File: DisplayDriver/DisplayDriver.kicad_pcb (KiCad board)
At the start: 2 copper layers, 1 part, among them U6 CH340N

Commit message: Design Doc 2 Final
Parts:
- removed U6: CH340N, Package_SO:SOP-8_3.9x4.9mm_P1.27mm
- added BOOT_SW: SW_Push_1P1T_NO_CK_PTS125Sx43PSMTR, Button_Switch_SMD:SW_Push_1P1T_NO_CK_PTS125Sx43PSMTR, F.Cu at (117.5, 38.5)
- added DOWN SW: SW_TL3330AF260QG, DisplayDriver:SW_TL3330AF260QG, F.Cu at (145.0, 69.5)
- added REF**: SOIC-20W_7.5x12.8mm_P1.27mm, Package_SO:SOIC-20W_7.5x12.8mm_P1.27mm, F.Cu at (70.8, 91.4)
- added REF**: LED_WS2812B_PLCC4_5.0x5.0mm_P3.2mm, LED_SMD:LED_WS2812B_PLCC4_5.0x5.0mm_P3.2mm, F.Cu at (173.5, 92.5)
- added REF**: LED_0603_1608Metric, LED_SMD:LED_0603_1608Metric, F.Cu at (240.5, 91.5)
- added REF**: SOIC-20W_7.5x12.8mm_P1.27mm, Package_SO:SOIC-20W_7.5x12.8mm_P1.27mm, F.Cu at (39.9, 91.9)
- added REF**: JST_PH_S3B-PH-K_1x03_P2.00mm_Horizontal, Connector_JST:JST_PH_S3B-PH-K_1x03_P2.00mm_Horizontal, F.Cu at (128.0, 91.5)
- added REF**: XCVR_ESP32-WROVER-B__16MB_, DisplayDriver:XCVR_ESP32-WROVER-B__16MB_, F.Cu at (47.0, 173.3)
- added REF**: IDC-Header_2x08_P2.54mm_Latch_Vertical, Connector_IDC:IDC-Header_2x08_P2.54mm_Latch_Vertical, F.Cu at (266.7, 31.1)
- added REF**: LED_0603_1608Metric, LED_SMD:LED_0603_1608Metric, F.Cu at (221.5, 91.5)
- added REF**: LED_0603_1608Metric, LED_SMD:LED_0603_1608Metric, F.Cu at (201.5, 91.5)
- added REF**: IDC-Header_2x08_P2.54mm_Latch_Vertical, Connector_IDC:IDC-Header_2x08_P2.54mm_Latch_Vertical, F.Cu at (108.0, 151.7)
- added REF**: PinHeader_1x11_P2.54mm_Vertical, Connector_PinHeader_2.54mm:PinHeader_1x11_P2.54mm_Vertical, F.Cu at (269.5, 74.7)
- added RESET SW: SW_TL3330AF260QG, DisplayDriver:SW_TL3330AF260QG, F.Cu at (173.6, 70.5)
- added UP SW: SW_TL3330AF260QG, DisplayDriver:SW_TL3330AF260QG, F.Cu at (119.5, 69.5)

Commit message: PCB commit pls
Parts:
- removed the REF** at (266.7, 31.1)
- removed the REF** at (108.0, 151.7)
- removed the REF** at (269.5, 74.7)
- added C2: C_0201_0603Metric, Capacitor_SMD:C_0201_0603Metric, F.Cu at (135.9, 42.9)
- added J1: SAMTEC_HTSS-108-01-G-D, DisplayDriver:SAMTEC_HTSS-108-01-G-D, F.Cu at (144.0, 143.0)
- added J2: PinHeader_1x11_P2.54mm_Vertical, Connector_PinHeader_2.54mm:PinHeader_1x11_P2.54mm_Vertical, F.Cu at (24.5, 140.7)
- added J3: SAMTEC_HTSS-108-01-G-D, DisplayDriver:SAMTEC_HTSS-108-01-G-D, F.Cu at (160.5, 174.4)
- added R1: R_0201_0603Metric, Resistor_SMD:R_0201_0603Metric, F.Cu at (135.9, 37.9)
- added R3: 10k, Resistor_SMD:R_0201_0603Metric, F.Cu at (97.2, 145.5)
- added SJ1: SolderJumper-3_P1.3mm_Open_Rounded, Jumper:SolderJumper-3_P1.3mm_Open_RoundedPad1.0x1.5mm_NumberLabels, F.Cu at (162.7, 150.5)
- added SJ2: SolderJumper-3_P1.3mm_Open_Rounded, Jumper:SolderJumper-3_P1.3mm_Open_RoundedPad1.0x1.5mm_NumberLabels, F.Cu at (90.2, 114.0)
- 3.3V LED-G: renamed from REF**
- 5V LED-G: renamed from REF**
- D15 LED-R: renamed from REF**
- DOWN1: renamed from DOWN SW
- RST1: renamed from RESET SW
- UP1: renamed from UP SW
- moved D15 LED-R 170.0 mm to (75.5, 50.5), turned to 90 degrees
- moved RST1 151.2 mm to (23.1, 84.6), turned to -90 degrees
- moved DOWN1 126.8 mm to (23.1, 104.6), turned to -90 degrees
- moved REF** 105.1 mm to (45.0, 27.0), turned to -90 degrees
- moved UP1 99.5 mm to (23.2, 94.6), turned to -90 degrees
- moved U1 83.7 mm to (70.5, 92.9)
- moved U3 76.9 mm to (111.0, 121.0)
- moved 5V LED-G 73.8 mm to (150.5, 71.5), turned to 90 degrees
- moved 3.3V LED-G 59.4 mm to (150.5, 61.0), turned to 90 degrees
- moved U2 40.6 mm to (111.2, 96.6)
- moved SW1 30.6 mm to (119.8, 69.0)
- moved neo_LED 20.9 mm to (178.7, 72.3), turned to -90 degrees
- renumbered BOOT_SW to SW1, REF** to U1, REF** to U2, REF** to U3, REF** to neo_LED
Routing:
- net (no net): track 0.00 -> 1102.3 mm

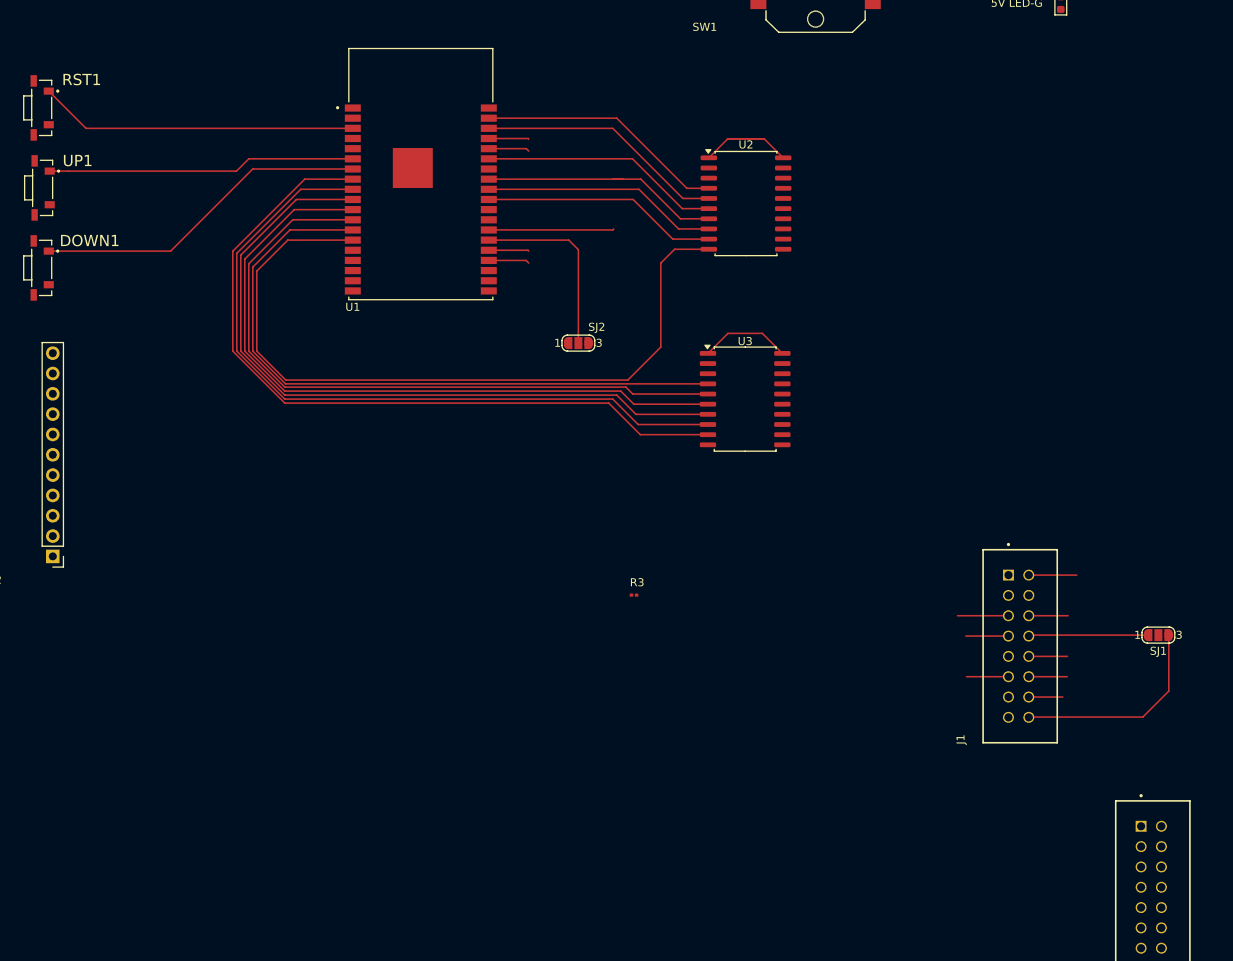
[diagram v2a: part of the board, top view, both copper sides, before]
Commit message: desktop to laptop
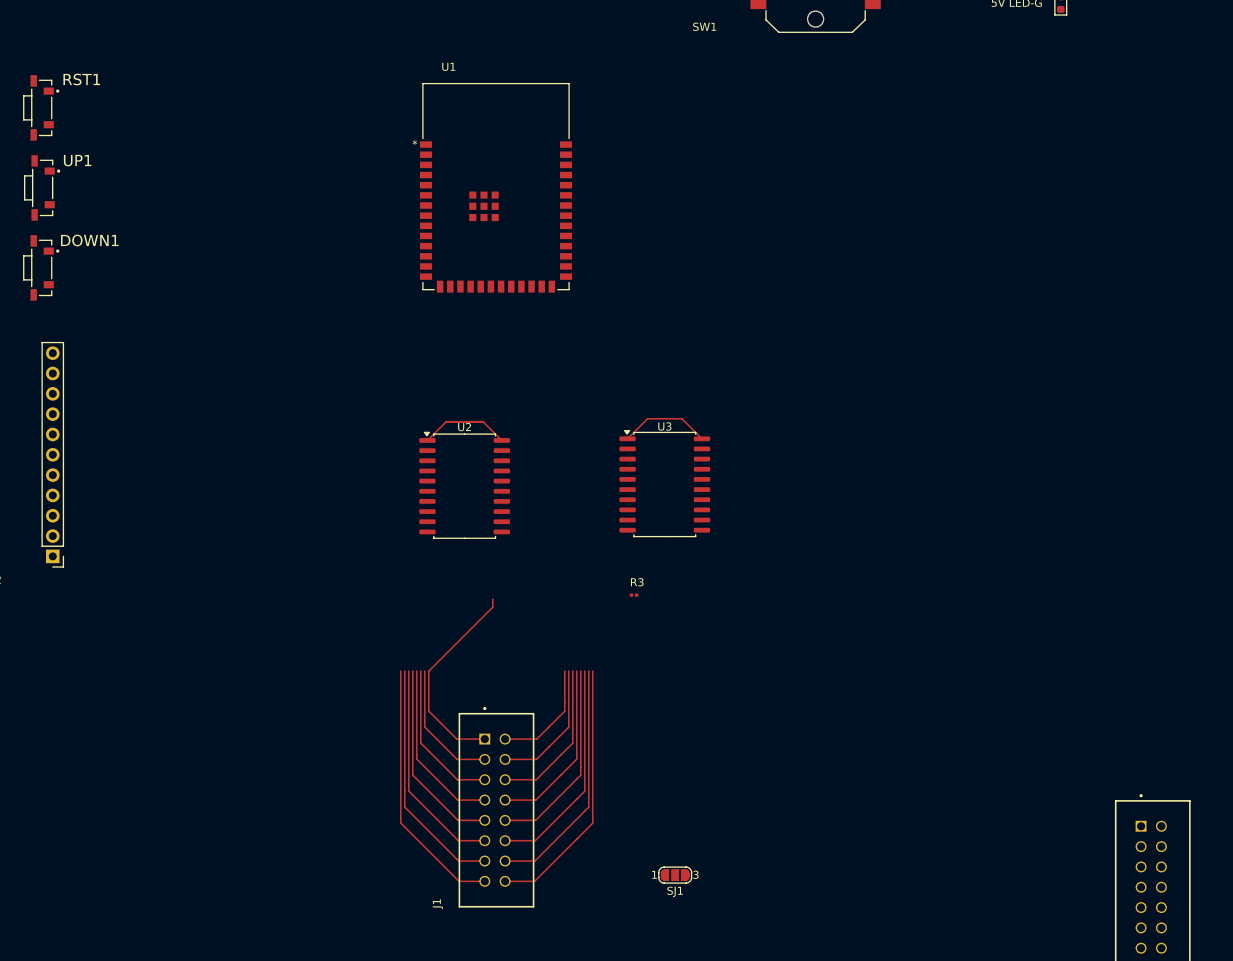
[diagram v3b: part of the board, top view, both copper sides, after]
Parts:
- removed SJ2: SolderJumper-3_P1.3mm_Open_Rounded, Jumper:SolderJumper-3_P1.3mm_Open_RoundedPad1.0x1.5mm_NumberLabels
- U1: value XCVR_ESP32-WROVER-B__16MB_ -> ESP32-S3-WROOM-1_EXP; footprint DisplayDriver:XCVR_ESP32-WROVER-B__16MB_ -> DisplayDriver:ESP32-S3-WROOM-1_EXP
- moved J1 68.6 mm to (78.5, 163.5)
- moved SJ1 67.4 mm to (102.3, 180.5)
- moved U2 49.9 mm to (76.0, 131.9)
- moved U3 14.7 mm to (101.0, 131.7)
- moved U1 9.53 mm to (79.9, 94.4)
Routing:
- net (no net): track 1102.3 -> 411.0 mm

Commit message: eod lab thurs
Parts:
- removed J2: PinHeader_1x11_P2.54mm_Vertical, Connector_PinHeader_2.54mm:PinHeader_1x11_P2.54mm_Vertical
- removed REF**: JST_PH_S3B-PH-K_1x03_P2.00mm_Horizontal, Connector_JST:JST_PH_S3B-PH-K_1x03_P2.00mm_Horizontal
- moved U3 41.4 mm to (111.0, 91.5)
- moved U2 40.5 mm to (111.0, 111.6)
- turned LED1 to 0 degrees
- renumbered neo_LED to LED1
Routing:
- net (no net): track 411.0 -> 579.0 mm, vias 0 -> 3

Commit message: halfway commit PCB
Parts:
- removed 3.3V LED-G: LED_0603_1608Metric, LED_SMD:LED_0603_1608Metric
- removed 5V LED-G: LED_0603_1608Metric, LED_SMD:LED_0603_1608Metric
- removed D15 LED-R: LED_0603_1608Metric, LED_SMD:LED_0603_1608Metric
- added C1: 0.1uF, Capacitor_SMD:C_0805_2012Metric_Pad1.18x1.45mm_HandSolder, F.Cu at (177.9, 95.6)
- added C10: 0.1uF, Capacitor_SMD:C_0805_2012Metric_Pad1.18x1.45mm_HandSolder, F.Cu at (182.7, 109.8)
- added C11: 10uF, Capacitor_SMD:C_0805_2012Metric_Pad1.18x1.45mm_HandSolder, F.Cu at (182.7, 114.5)
- added C12: 10uF, Capacitor_SMD:C_0805_2012Metric_Pad1.18x1.45mm_HandSolder, F.Cu at (182.7, 119.3)
- added C13: 10uF, Capacitor_SMD:C_0805_2012Metric_Pad1.18x1.45mm_HandSolder, F.Cu at (187.5, 95.6)
- added C14: 10uF, Capacitor_SMD:C_0805_2012Metric_Pad1.18x1.45mm_HandSolder, F.Cu at (187.5, 100.3)
- added C15: 0.1uF, Capacitor_SMD:C_0805_2012Metric_Pad1.18x1.45mm_HandSolder, F.Cu at (187.5, 105.0)
- added C16: 0.1uF, Capacitor_SMD:C_0805_2012Metric_Pad1.18x1.45mm_HandSolder, F.Cu at (187.5, 109.8)
- added C3: 10uF, Capacitor_SMD:C_0805_2012Metric_Pad1.18x1.45mm_HandSolder, F.Cu at (177.9, 105.0)
- added C4: 10uF, Capacitor_SMD:C_0805_2012Metric_Pad1.18x1.45mm_HandSolder, F.Cu at (177.9, 109.8)
- added C5: 0.1uF, Capacitor_SMD:C_0805_2012Metric_Pad1.18x1.45mm_HandSolder, F.Cu at (177.9, 114.5)
- added C6: 1uF, Capacitor_SMD:C_0805_2012Metric_Pad1.18x1.45mm_HandSolder, F.Cu at (177.9, 119.3)
- added C7: 1uF, Capacitor_SMD:C_0805_2012Metric_Pad1.18x1.45mm_HandSolder, F.Cu at (182.7, 95.6)
- added C8: 10uF, Capacitor_SMD:C_0805_2012Metric_Pad1.18x1.45mm_HandSolder, F.Cu at (182.7, 100.3)
- added C9: 0.1uF, Capacitor_SMD:C_0805_2012Metric_Pad1.18x1.45mm_HandSolder, F.Cu at (182.7, 105.0)
- added L1: RED, LED_SMD:LED_0603_1608Metric, F.Cu at (167.9, 95.0)
- added L2: GREEN, LED_SMD:LED_0603_1608Metric, F.Cu at (168.0, 99.2)
- added L3: GREEN, LED_SMD:LED_0603_1608Metric, F.Cu at (168.0, 104.0)
- added PC1: 100uF/6.3V, Capacitor_SMD:C_0805_2012Metric_Pad1.18x1.45mm_HandSolder, F.Cu at (187.5, 114.5)
- added R2: 10K, Resistor_SMD:R_0805_2012Metric_Pad1.20x1.40mm_HandSolder, F.Cu at (196.3, 99.8)
- added R4: 10K, Resistor_SMD:R_0805_2012Metric_Pad1.20x1.40mm_HandSolder, F.Cu at (196.3, 109.2)
- added R5: 10K, Resistor_SMD:R_0805_2012Metric_Pad1.20x1.40mm_HandSolder, F.Cu at (196.3, 114.0)
- added R6: 10K, Resistor_SMD:R_0805_2012Metric_Pad1.20x1.40mm_HandSolder, F.Cu at (196.3, 118.8)
- added R7: Resistor_SMD:R_0805_2012Metric_Pad1.20x1.40mm_HandSolder, Resistor_SMD:R_0805_2012Metric_Pad1.20x1.40mm_HandSolder, F.Cu at (196.3, 123.5)
- added R8: 5.1k, Resistor_SMD:R_0805_2012Metric_Pad1.20x1.40mm_HandSolder, F.Cu at (196.3, 128.5)
- added R8: 5.1k, Resistor_SMD:R_0805_2012Metric_Pad1.20x1.40mm_HandSolder, F.Cu at (203.8, 128.5)
- added R8: 5.1k, Resistor_SMD:R_0805_2012Metric_Pad1.20x1.40mm_HandSolder, F.Cu at (200.0, 128.5)
- added R8: 5.1k, Resistor_SMD:R_0805_2012Metric_Pad1.20x1.40mm_HandSolder, F.Cu at (207.5, 128.5)
- added R9: 22, Resistor_SMD:R_0805_2012Metric_Pad1.20x1.40mm_HandSolder, F.Cu at (196.3, 133.5)
- added R9: 22, Resistor_SMD:R_0805_2012Metric_Pad1.20x1.40mm_HandSolder, F.Cu at (207.5, 133.5)
- added R9: 22, Resistor_SMD:R_0805_2012Metric_Pad1.20x1.40mm_HandSolder, F.Cu at (199.8, 133.5)
- added R9: 22, Resistor_SMD:R_0805_2012Metric_Pad1.20x1.40mm_HandSolder, F.Cu at (203.5, 133.5)
- added U4: AP2112K-3.3TRG1, DisplayDriver:SOT95P285X140-5N, F.Cu at (90.7, 111.7)
- added U5: STUSB4500QTR, Package_DFN_QFN:QFN-24-1EP_4x4mm_P0.5mm_EP2.7x2.7mm, F.Cu at (83.7, 110.8)
- added X1: CUI_UJ20-C-H-G-SMT-TR, DisplayDriver:CUI_UJ20-C-H-G-SMT-TR, F.Cu at (85.0, 123.0)
- added X2: CUI_UJ20-C-H-G-SMT-TR, DisplayDriver:CUI_UJ20-C-H-G-SMT-TR, F.Cu at (149.2, 56.0)
- C2: value C_0201_0603Metric -> 10uF; footprint Capacitor_SMD:C_0201_0603Metric -> Capacitor_SMD:C_0805_2012Metric_Pad1.18x1.45mm_HandSolder
- R1: value R_0201_0603Metric -> 10K; footprint Resistor_SMD:R_0201_0603Metric -> Resistor_SMD:R_0805_2012Metric_Pad1.20x1.40mm_HandSolder
- R3: value 10k -> 10K; footprint Resistor_SMD:R_0201_0603Metric -> Resistor_SMD:R_0805_2012Metric_Pad1.20x1.40mm_HandSolder
- SW1: value SW_Push_1P1T_NO_CK_PTS125Sx43PSMTR -> Generic (Lab Kit); footprint Button_Switch_SMD:SW_Push_1P1T_NO_CK_PTS125Sx43PSMTR -> Button_Switch_THT:SW_PUSH_6mm
- U1: value ESP32-S3-WROOM-1_EXP -> ESP32-S3-WROOM-1; footprint DisplayDriver:ESP32-S3-WROOM-1_EXP -> RF_Module:ESP32-S3-WROOM-1
- moved R3 107.3 mm to (196.3, 104.5)
- moved R1 83.2 mm to (196.3, 95.1), turned to 0 degrees
- moved J1 78.7 mm to (128.7, 102.8)
- moved C2 71.1 mm to (177.9, 100.3), turned to 0 degrees
- moved SJ1 70.6 mm to (137.7, 119.3), turned to -90 degrees
- moved DOWN1 57.1 mm to (79.9, 98.4)
- moved RST1 57.1 mm to (79.9, 78.4)
- moved UP1 57.1 mm to (80.0, 88.4)
- moved LED1 39.2 mm to (170.4, 110.7)
- moved J3 35.5 mm to (125.2, 171.1)
- moved U1 27.6 mm to (102.0, 77.8)
- moved U3 27.2 mm to (134.6, 78.0)
- moved SW1 27.0 mm to (128.0, 94.8), turned to 90 degrees
- moved U2 1.32 mm to (111.4, 110.3)
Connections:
- C2 pad 1: (no net) -> GND
- C2 pad 2: (no net) -> +5V
- R1 pad 1: (no net) -> /BOOT0
- R1 pad 2: (no net) -> 3.3V
- R3 pad 1: (no net) -> 3.3V
- R3 pad 2: (no net) -> unconnected-(R3-Pad2)
- U1 pad 1: (no net) -> GND
- U1 pad 10: (no net) -> /OE_3V
- U1 pad 11: (no net) -> /B2_3V
- U1 pad 12: (no net) -> /G2_3V
- U1 pad 13: (no net) -> /D1-
- U1 pad 14: (no net) -> /D1+
- U1 pad 15: (no net) -> /R2_3V
- U1 pad 16: (no net) -> /NC8
- U1 pad 17: (no net) -> /B1_3V
- U1 pad 18: (no net) -> /G1_3V
- U1 pad 19: (no net) -> /R1_3V
- U1 pad 2: (no net) -> 3.3V
- U1 pad 20: (no net) -> /LAT_3V
- U1 pad 21: (no net) -> /D13
- U1 pad 22: (no net) -> /NC3
- U1 pad 23: (no net) -> /NC9
- U1 pad 24: (no net) -> /NC7
- U1 pad 25: (no net) -> /NC6
- U1 pad 26: (no net) -> /NEOPIX
- U1 pad 27: (no net) -> /BOOT0
- U1 pad 28: (no net) -> unconnected-(U1-IO35-Pad28)
- U1 pad 29: (no net) -> unconnected-(U1-IO36-Pad29)
- U1 pad 3: (no net) -> /~{RESET}
- U1 pad 30: (no net) -> unconnected-(U1-IO37-Pad30)
- U1 pad 31: (no net) -> /ADDRA_3V
- U1 pad 32: (no net) -> /ADDRB_3V
- U1 pad 33: (no net) -> /ADDRC_3V
- U1 pad 34: (no net) -> /ADDRD_3V
- U1 pad 35: (no net) -> /ADDRE_3V
- U1 pad 36: (no net) -> /UART_RX
- U1 pad 37: (no net) -> /UART_TX
- U1 pad 38: (no net) -> /DOWN
- U1 pad 39: (no net) -> /UP
- U1 pad 4: (no net) -> /CLK_3V
- U1 pad 40: (no net) -> GND
- U1 pad 41: (no net) -> GND
- U1 pad 5: (no net) -> /NC
- U1 pad 6: (no net) -> /NC1
- U1 pad 7: (no net) -> /NC2
- U1 pad 8: (no net) -> /NC4
- U1 pad 9: (no net) -> /NC5
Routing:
- net (no net): track 579.0 -> 520.4 mm, vias 3 -> 2
- net /OE_3V: track 0.00 -> 44.8 mm
- net /CLK_3V: track 0.00 -> 43.8 mm, vias 0 -> 2
- net /B2_3V: track 0.00 -> 41.7 mm
- net /G2_3V: track 0.00 -> 38.6 mm
- net /R2_3V: track 0.00 -> 28.0 mm
- net /B1_3V: track 0.00 -> 25.8 mm
- net /G1_3V: track 0.00 -> 23.9 mm
- net /R1_3V: track 0.00 -> 22.1 mm
- net /LAT_3V: track 0.00 -> 20.3 mm
- net /ADDRC_3V: track 0.00 -> 19.9 mm
- net /ADDRE_3V: track 0.00 -> 19.9 mm
- net /ADDRD_3V: track 0.00 -> 19.9 mm
- net /ADDRA_3V: track 0.00 -> 19.9 mm
- net /ADDRB_3V: track 0.00 -> 19.9 mm
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
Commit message: pcb
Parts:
- J1: value SAMTEC_HTSS-108-01-G-D -> HTSS-108-01-G-D; footprint DisplayDriver:SAMTEC_HTSS-108-01-G-D -> Connector_IDC:IDC-Header_2x08_P2.54mm_Vertical
- U2, U3: value SOIC-20W_7.5x12.8mm_P1.27mm -> 74AHCT245
- moved SW1 76.9 mm to (192.8, 53.2), turned to 0 degrees
- moved C1 39.5 mm to (202.8, 64.8)
- moved C10 39.5 mm to (207.6, 79.0)
- moved C11 39.5 mm to (207.6, 83.7)
- moved C12 39.5 mm to (207.6, 88.5)
- moved C13 39.5 mm to (212.4, 64.8)
- moved C14 39.5 mm to (212.4, 69.5)
- moved C15 39.5 mm to (212.4, 74.2)
- moved C16 39.5 mm to (212.4, 79.0)
- moved C2 39.5 mm to (202.8, 69.5)
- moved C3 39.5 mm to (202.8, 74.2)
- moved C4 39.5 mm to (202.8, 79.0)
- moved C5 39.5 mm to (202.8, 83.7)
- moved C6 39.5 mm to (202.8, 88.5)
- moved C7 39.5 mm to (207.6, 64.8)
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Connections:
- J1 pad 01: (no net) -> /M1_R1
- J1 pad 02: (no net) -> /M1_G1
- J1 pad 03: (no net) -> /M1_B1
- J1 pad 04: (no net) -> GND
- J1 pad 05: (no net) -> /M1_R2
- J1 pad 06: (no net) -> /M1_G2
- J1 pad 07: (no net) -> /M1_B2
- J1 pad 08: (no net) -> /M1_E8
- J1 pad 09: (no net) -> /M1_A
- J1 pad 10: (no net) -> /M1_B
- J1 pad 11: (no net) -> /M1_C
- J1 pad 12: (no net) -> /M1_D
- J1 pad 13: (no net) -> /CLK
- J1 pad 14: (no net) -> /LAT
- J1 pad 15: (no net) -> /OE
- J1 pad 16: (no net) -> /M1_E16
- R8 pad 1: (no net) -> GND (x3)
- R8 pad 2: (no net) -> GND (x3)
- R9 pad 1: (no net) -> Net-(X1-DN1) (x3)
- R9 pad 2: (no net) -> Net-(R9B-1) (x3)
- SJ1 pad 3: (no net) -> /M1_E16
- U2 pad 1: (no net) -> +5V
- U2 pad 10: (no net) -> GND
- U2 pad 11: (no net) -> /OE
- U2 pad 12: (no net) -> /M1_B2
- U2 pad 13: (no net) -> /M1_G2
- U2 pad 14: (no net) -> /M1_R2
- U2 pad 15: (no net) -> /M1_B1
- U2 pad 16: (no net) -> /M1_G1
- U2 pad 17: (no net) -> /M1_R1
- U2 pad 18: (no net) -> /LAT
- U2 pad 19: (no net) -> GND
- U2 pad 2: (no net) -> /LAT_3V
- U2 pad 20: (no net) -> +5V
- U2 pad 3: (no net) -> /R1_3V
- U2 pad 4: (no net) -> /G1_3V
- U2 pad 5: (no net) -> /B1_3V
- U2 pad 6: (no net) -> /R2_3V
- U2 pad 7: (no net) -> /G2_3V
- U2 pad 8: (no net) -> /B2_3V
- U2 pad 9: (no net) -> /OE_3V
- U3 pad 1: (no net) -> +5V
- U3 pad 10: (no net) -> GND
- U3 pad 11: (no net) -> /M1_A
- U3 pad 12: (no net) -> /M1_B
- U3 pad 13: (no net) -> /M1_C
- U3 pad 14: (no net) -> /M1_D
- U3 pad 15: (no net) -> /M1_E
- U3 pad 16: (no net) -> /CLK
- U3 pad 17: (no net) -> unconnected-(U3-B2-Pad17)
- U3 pad 18: (no net) -> unconnected-(U3-B1-Pad18)
- U3 pad 19: (no net) -> GND
- U3 pad 2: (no net) -> GND
- U3 pad 20: (no net) -> +5V
- U3 pad 3: (no net) -> GND
- U3 pad 4: (no net) -> /CLK_3V
- U3 pad 5: (no net) -> /ADDRE_3V
- U3 pad 6: (no net) -> /ADDRD_3V
- U3 pad 7: (no net) -> /ADDRC_3V
- U3 pad 8: (no net) -> /ADDRB_3V
- U3 pad 9: (no net) -> /ADDRA_3V
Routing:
- net (no net): track 520.4 -> 86.3 mm, vias 2 -> 0
- net /CLK: track 0.00 -> 54.5 mm
- net /M1_E: track 0.00 -> 46.4 mm, vias 0 -> 2
- net /M1_C: track 0.00 -> 45.5 mm
- net /M1_D: track 0.00 -> 45.4 mm
- net /M1_A: track 0.00 -> 39.7 mm
- net /M1_B: track 0.00 -> 39.5 mm
- net /LAT: track 0.00 -> 23.0 mm, vias 0 -> 1
- net /M1_E8: track 0.00 -> 18.3 mm, vias 0 -> 1
- net /M1_G1: track 0.00 -> 18.0 mm
- net /M1_G2: track 0.00 -> 17.5 mm
- net /M1_B1: track 0.00 -> 14.9 mm
- net /M1_R1: track 0.00 -> 14.9 mm
- net /OE: track 0.00 -> 14.6 mm
- net /M1_R2: track 0.00 -> 14.4 mm
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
